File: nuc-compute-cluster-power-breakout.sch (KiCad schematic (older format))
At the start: 20 parts, among them J10 10107844-002LF, J2 BM04B-SRSS-TB-LF-SN, J3 BM04B-SRSS-TB-LF-SN, J5 430450812, J6 430450812, J7 430450812, J8 430450812, J9 430450812, Q11 BC856,215

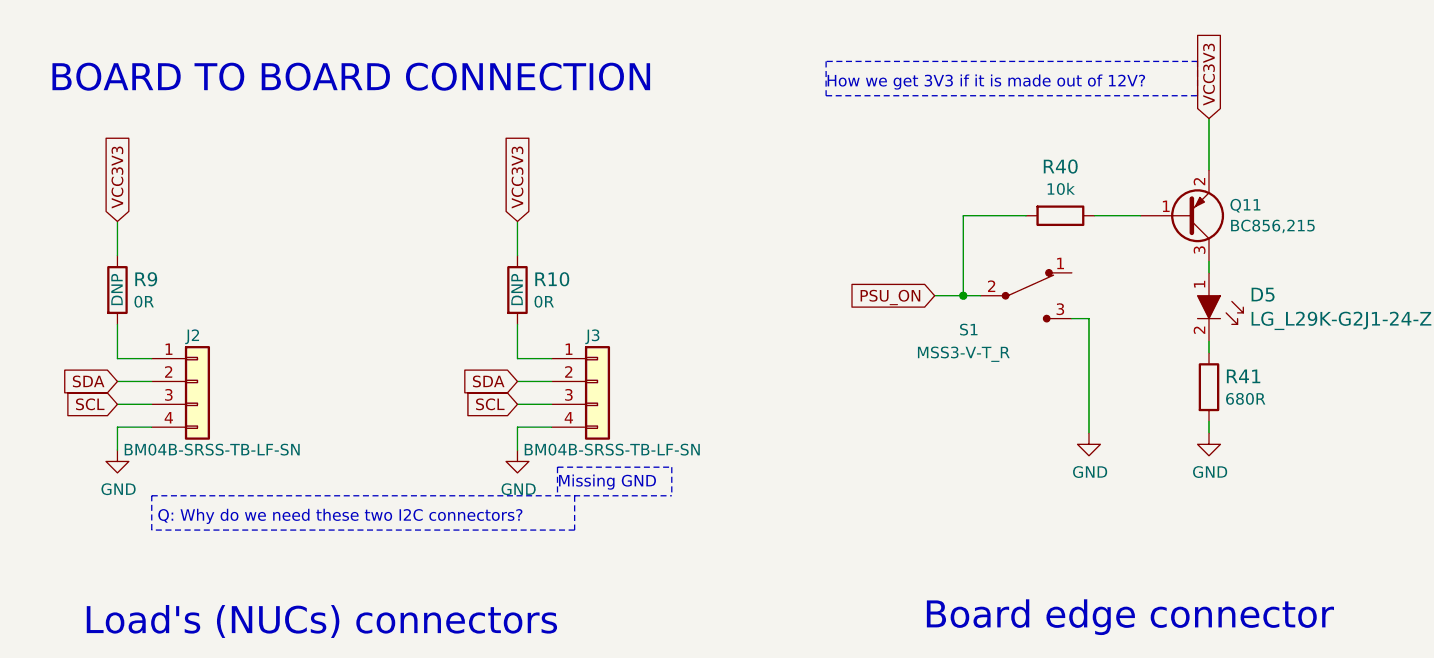
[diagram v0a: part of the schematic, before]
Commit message: Schematic visual update
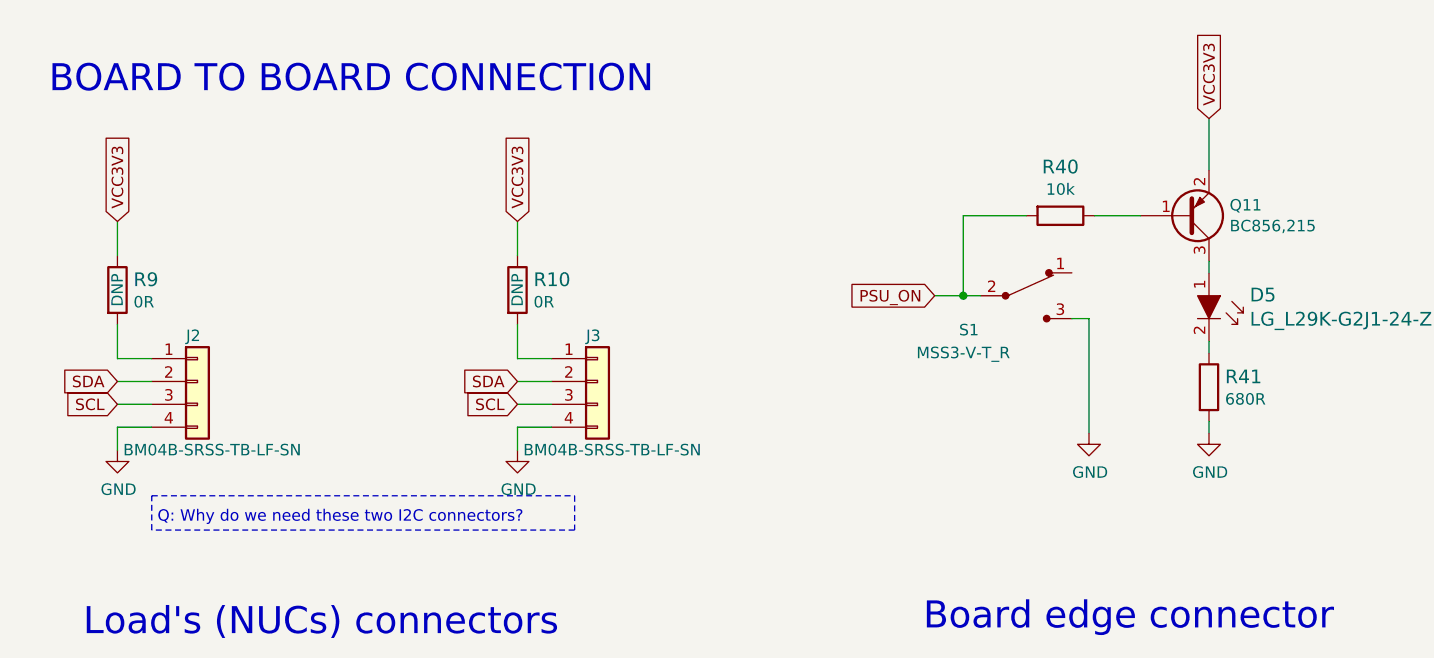
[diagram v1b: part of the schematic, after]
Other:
- note removed: "How we get 3V3 if it is made out of 12V?"
- note removed: "Missing GND"
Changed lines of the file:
@@
 Wire Wire Line
 	7800 6000 7800 5775
-Text Notes 3350 2600 0    50   ~ 0
-Missing GND
-Text Notes 4525 850  0    50   ~ 0
-How we get 3V3 if it is made out of 12V?
 Text Notes 5275 5700 0    50   ~ 0
 Add tespads for the signall pins
@@
 Wire Notes Line
 	1575 2775 1575 2625
-Wire Notes Line
-	3350 2500 3850 2500
-Wire Notes Line
-	3850 2500 3850 2625
-Wire Notes Line
-	3350 2500 3350 2625
-Wire Notes Line
-	1575 2625 3850 2625
-Wire Notes Line
-	4525 725  4525 875
-Wire Notes Line
-	4525 875  6150 875
-Wire Notes Line
-	6150 875  6150 725
-Wire Notes Line
-	6150 725  4525 725
 Wire Notes Line
 	5250 5600 5250 5750
@@
 	1    0    0    -1
 $EndComp
+Wire Notes Line
+	1575 2625 3425 2625
 $EndSCHEMATC

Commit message: Improvements after review
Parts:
- added TP_S1, TP_S10, TP_S11, TP_S12, TP_S16, TP_S17, TP_S18, TP_S19, TP_S2, TP_S20, TP_S21, TP_S22, TP_S23, TP_S24, TP_S3, TP_S4, TP_S5, TP_S6, TP_S7, TP_S8, TP_S9, TP_S_ON: TP_SMD1MM, antmicro-footprints:Testpoint_smd_1mm, symbol antmicroTestPoints:TP_SMD1MM
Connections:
- net PSU_ON: now also TP_S_ON.1; no longer J10.S13, J10.S14, J10.S15
- net at J10.S1: now also TP_S1.1
- net at J10.S10: now also TP_S10.1
- net at J10.S11: now also TP_S11.1
- net at J10.S12: now also TP_S12.1
- net at J10.S16: now also TP_S16.1
- net at J10.S17: now also TP_S17.1
- net at J10.S18: now also TP_S18.1
- net at J10.S19: now also TP_S19.1
- net at J10.S2: now also TP_S2.1
- net at J10.S20: now also TP_S20.1
- net at J10.S21: now also TP_S21.1
- net at J10.S22: now also TP_S22.1
- net at J10.S23: now also TP_S23.1
- net at J10.S24: now also TP_S24.1
- net at J10.S3: now also TP_S3.1
- net at J10.S4: now also TP_S4.1
- net at J10.S5: now also TP_S5.1
- net at J10.S6: now also TP_S6.1
- net at J10.S7: now also TP_S7.1
- net at J10.S8: now also TP_S8.1
- net at J10.S9: now also TP_S9.1
- new net: J10.S13, J10.S14, J10.S15
- no-connect marks 22 -> 1
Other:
- note removed: "Add tespads for the signall pins"
- note removed: "Q: Why do we need these two I2C connectors?"

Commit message: Patches after 2nd revision
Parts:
- removed MP1: PCB_Mount_Hole_3mm_6mm_pad, nuc-compute-cluster-power-breakout-footprints:mounting-hole-3.2mm, symbol nuc-compute-cluster-power-breakout:PCB_Mount_Hole_3mm_6mm_pad
- J2: DNP (none) -> DNP
- renumbered MP5 to MP1, TP_S_ON to TP_S_ON1
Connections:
- net PSU_ON: now also J10.S13, J10.S14, J10.S15
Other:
- moved on the sheet: MP1
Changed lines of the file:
@@
 F 4 "BM04B-SRSS-TB(LF)(SN) " H 1675 1925 50  0001 L CNN "MPN"
 F 5 "JST" H 1675 1825 50  0001 L CNN "Manufacturer"
+F 6 "DNP" V 1875 2375 50  0000 C CNN "DNP"
 	1    1775 2275
 	1    0    0    -1
@@
 	6200 975  6200 1200
 $Comp
-L nuc-compute-cluster-power-breakout:PCB_Mount_Hole_3mm_6mm_pad MP1
-U 1 1 624D5C25
-P 8575 5375
-F 0 "MP1" H 8643 5720 50  0000 C CNN
-F 1 "PCB_Mount_Hole_3mm_6mm_pad" H 8643 5629 50  0000 C CNN
-F 2 "nuc-compute-cluster-power-breakout-footprints:mounting-hole-3.2mm" H 9375 6075 50  0001 C CNN
-F 3 "" H 9525 6175 50  0001 C CNN
-	1    8575 5375
-	1    0    0    -1
-$EndComp
-$Comp
-L nuc-compute-cluster-power-breakout:PCB_Mount_Hole_3mm_6mm_pad MP3
-U 1 1 624DA217
-P 9925 5375
-F 0 "MP3" H 9993 5720 50  0000 C CNN
-F 1 "PCB_Mount_Hole_3mm_6mm_pad" H 9993 5629 50  0000 C CNN
-F 2 "nuc-compute-cluster-power-breakout-footprints:mounting-hole-3.2mm" H 10725 6075 50  0001 C CNN
-F 3 "" H 10875 6175 50  0001 C CNN
-	1    9925 5375
-	1    0    0    -1
-$EndComp
-$Comp
 L nuc-compute-cluster-power-breakout:PCB_Mount_Hole_3mm_6mm_pad MP2
 U 1 1 624E49B1
@@
 $EndComp
 $Comp
-L nuc-compute-cluster-power-breakout:GND #PWR072
-U 1 1 624EAD7E
-P 8875 5575
-F 0 "#PWR072" H 8875 5325 50  0001 C CNN
-F 1 "GND" H 8880 5402 50  0000 C CNN
-F 2 "" H 8875 5575 50  0001 C CNN
-F 3 "" H 8875 5575 50  0001 C CNN
-	1    8875 5575
-	1    0    0    -1
-$EndComp
-$Comp
 L nuc-compute-cluster-power-breakout:GND #PWR074
 U 1 1 624EB150
@@
 	10225 5375 10225 5575
 Wire Wire Line
-	8875 5575 8875 5375
-Wire Wire Line
 	10225 6125 10225 6300
 Wire Wire Line
 	8875 6125 8875 6300
 $Comp
-L nuc-compute-cluster-power-breakout:PCB_Mount_Hole_3mm_6mm_pad MP5
+L nuc-compute-cluster-power-breakout:PCB_Mount_Hole_3mm_6mm_pad MP1
 U 1 1 62504F51
-P 7500 5775
-F 0 "MP5" H 7568 6120 50  0000 C CNN
-F 1 "PCB_Mount_Hole_3mm_6mm_pad" H 7568 6029 50  0000 C CNN
-F 2 "nuc-compute-cluster-power-breakout-footprints:mounting-hole-3.2mm" H 8300 6475 50  0001 C CNN
-F 3 "" H 8450 6575 50  0001 C CNN
-	1    7500 5775
+P 8575 5375
+F 0 "MP1" H 8643 5720 50  0000 C CNN
+F 1 "PCB_Mount_Hole_3mm_6mm_pad" H 8643 5629 50  0000 C CNN
+F 2 "nuc-compute-cluster-power-breakout-footprints:mounting-hole-3.2mm" H 9375 6075 50  0001 C CNN
+F 3 "" H 9525 6175 50  0001 C CNN
+	1    8575 5375
 	1    0    0    -1
 $EndComp
@@
 L nuc-compute-cluster-power-breakout:GND #PWR0106
 U 1 1 6250AA38
-P 7800 6000
-F 0 "#PWR0106" H 7800 5750 50  0001 C CNN
-F 1 "GND" H 7805 5827 50  0000 C CNN
-F 2 "" H 7800 6000 50  0001 C CNN
-F 3 "" H 7800 6000 50  0001 C CNN
-	1    7800 6000
+P 8875 5575
+F 0 "#PWR0106" H 8875 5325 50  0001 C CNN
+F 1 "GND" H 8880 5402 50  0000 C CNN
+F 2 "" H 8875 5575 50  0001 C CNN
+F 3 "" H 8875 5575 50  0001 C CNN
+	1    8875 5575
 	1    0    0    -1
 $EndComp
-Wire Wire Line
-	7800 6000 7800 5775
 $Comp
-L nuc-compute-cluster-power-breakout:GND #PWR?
+L nuc-compute-cluster-power-breakout:GND #PWR0107
 U 1 1 624F066D
 P 3175 2425
-F 0 "#PWR?" H 3175 2175 50  0001 C CNN
+F 0 "#PWR0107" H 3175 2175 50  0001 C CNN
 F 1 "GND" H 3180 2252 50  0000 C CNN
 F 2 "" H 3175 2425 50  0001 C CNN
@@
 	5175 5400 5300 5400
 $Comp
-L antmicroTestPoints:TP_SMD1MM TP_S_ON
+L antmicroTestPoints:TP_SMD1MM TP_S_ON1
 U 1 1 625B2FF0
 P 6725 5400
-F 0 "TP_S_ON" H 6775 5400 50  0000 L CNN
+F 0 "TP_S_ON1" H 6775 5400 50  0000 L CNN
 F 1 "TP_SMD1MM" H 6725 5300 50  0001 C CNN
 F 2 "antmicro-footprints:Testpoint_smd_1mm" H 6925 5600 60  0001 L CNN
@@
 	1    0    0    -1
 $EndComp
-Wire Wire Line
-	6725 5300 6525 5300
 Connection ~ 6725 5300
 Wire Wire Line
 	6725 5300 6900 5300
+Wire Wire Line
+	6500 5300 6725 5300
+$Comp
+L nuc-compute-cluster-power-breakout:PCB_Mount_Hole_3mm_6mm_pad MP3
+U 1 1 624DA217
+P 9925 5375
+F 0 "MP3" H 9993 5720 50  0000 C CNN
+F 1 "PCB_Mount_Hole_3mm_6mm_pad" H 9993 5629 50  0000 C CNN
+F 2 "nuc-compute-cluster-power-breakout-footprints:mounting-hole-3.2mm" H 10725 6075 50  0001 C CNN
+F 3 "" H 10875 6175 50  0001 C CNN
+	1    9925 5375
+	1    0    0    -1
+$EndComp
+Wire Wire Line
+	8875 5575 8875 5375
 $EndSCHEMATC

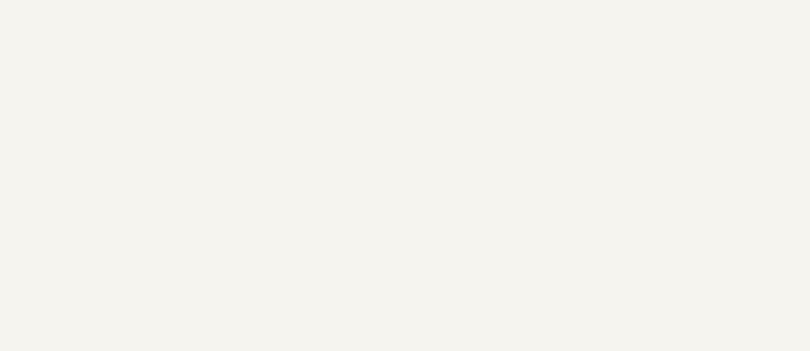
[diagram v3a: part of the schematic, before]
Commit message: Added board cut-out. Logos replacement
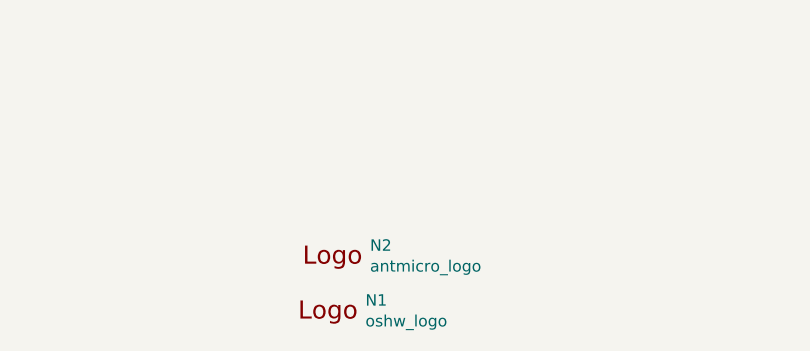
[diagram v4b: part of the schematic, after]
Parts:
- added N1: oshw_logo, antmicro-footprints:OSHW-Logo_7.5x8mm_Mask, symbol antmicroMechanicalParts:oshw_logo
- added N2: antmicro_logo, antmicro-footprints:antmicro-logo_scaled_20mm_mask, symbol antmicroMechanicalParts:antmicro_logo
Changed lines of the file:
@@
 Wire Wire Line
 	8875 5575 8875 5375
+$Comp
+L antmicroMechanicalParts:antmicro_logo N2
+U 1 1 62508F0C
+P 6075 7100
+F 0 "N2" H 6289 7193 50  0000 L CNN
+F 1 "antmicro_logo" H 6289 7102 50  0000 L CNN
+F 2 "antmicro-footprints:antmicro-logo_scaled_20mm_mask" H 5975 7350 50  0001 C CNN
+F 3 "" H 6075 7450 50  0001 C CNN
+	1    6075 7100
+	1    0    0    -1
+$EndComp
+$Comp
+L antmicroMechanicalParts:oshw_logo N1
+U 1 1 6250A4B1
+P 6075 7250
+F 0 "N1" H 6269 7253 50  0000 L CNN
+F 1 "oshw_logo" H 6269 7162 50  0000 L CNN
+F 2 "antmicro-footprints:OSHW-Logo_7.5x8mm_Mask" H 6095 7010 50  0001 C CNN
+F 3 "" H 6075 7250 50  0001 C CNN
+	1    6075 7250
+	1    0    0    -1
+$EndComp
 $EndSCHEMATC

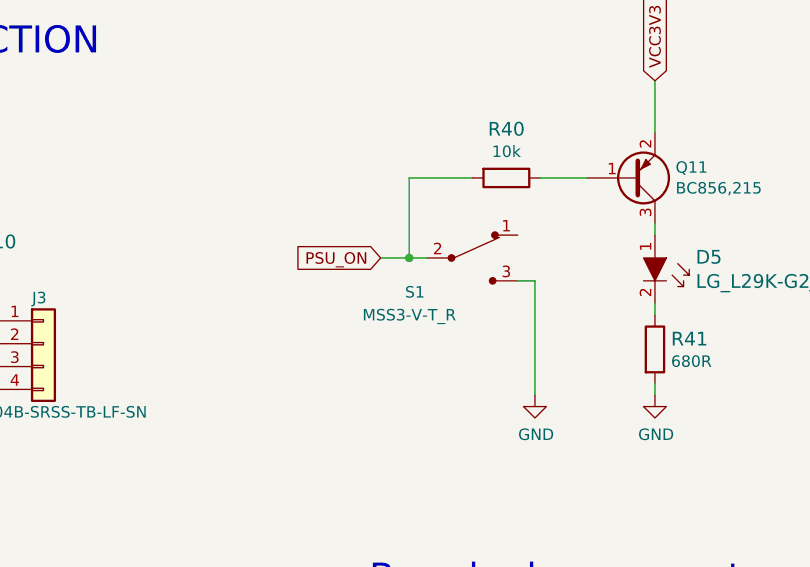
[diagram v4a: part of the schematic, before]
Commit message: Add R45 to implement ALWAYS ON feature
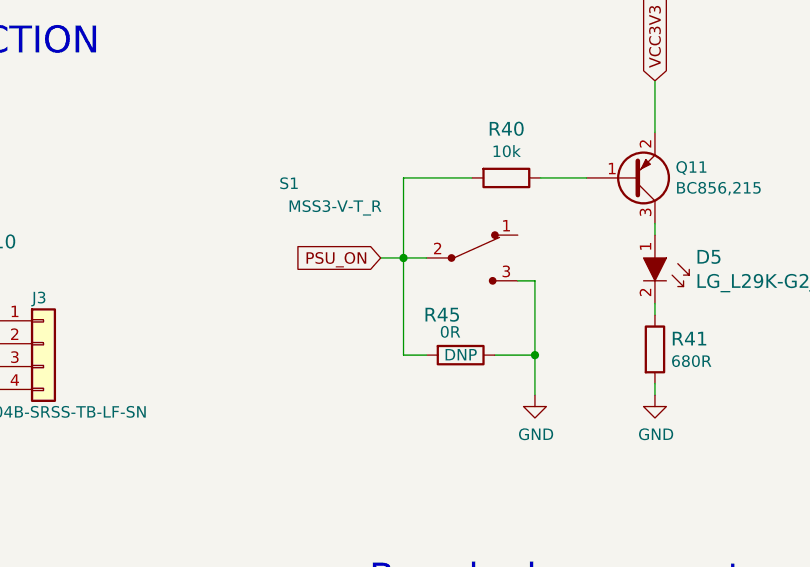
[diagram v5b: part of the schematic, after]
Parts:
- added R45: R_0R_0402, nuc-compute-cluster-power-breakout-footprints:0402-res, symbol nuc-compute-cluster-power-breakout:R_0R_0402
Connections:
- net GND: now also R45.1
- net PSU_ON: now also R45.2
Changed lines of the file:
@@
 U 1 1 6270AED7
 P 5400 1750
-F 0 "S1" H 5150 1600 50  0000 C CNN
-F 1 "MSS3-V-T_R" H 5125 1500 50  0000 C CNN
+F 0 "S1" H 4600 2075 50  0000 C CNN
+F 1 "MSS3-V-T_R" H 4800 1975 50  0000 C CNN
 F 2 "nuc-compute-cluster-power-breakout-footprints:Switch_Slide_MSS3" H 5600 1950 50  0001 L CNN
 F 3 "https://pl.mouser.com/datasheet/2/910/605_MSS34-1571494.pdf" H 5600 2050 60  0001 L CNN
@@
 $EndComp
 Wire Wire Line
-	5000 1750 5125 1750
+	5000 1750 5100 1750
 Wire Wire Line
 	5675 1850 5600 1850
 Wire Wire Line
-	5125 1750 5125 1400
-Connection ~ 5125 1750
-Wire Wire Line
-	5125 1750 5200 1750
+	5100 1750 5100 1400
+Connection ~ 5100 1750
+Wire Wire Line
+	5100 1750 5200 1750
 $Comp
 L nuc-compute-cluster-power-breakout:GND #PWR071
@@
 $EndComp
 Wire Wire Line
-	5125 1400 5400 1400
+	5100 1400 5400 1400
 Wire Wire Line
 	5700 1400 5900 1400
@@
 $EndComp
 Wire Wire Line
-	5675 1850 5675 2350
+	5675 1850 5675 2175
 $Comp
 L nuc-compute-cluster-power-breakout:BC856,215 Q11
@@
 	1    0    0    -1
 $EndComp
+$Comp
+L nuc-compute-cluster-power-breakout:R_0R_0402 R45
+U 1 1 6263D1AF
+P 5350 2175
+F 0 "R45" H 5350 2000 60  0000 L CNN
+F 1 "R_0R_0402" H 5350 2025 60  0001 C CNN
+F 2 "nuc-compute-cluster-power-breakout-footprints:0402-res" H 5550 2375 60  0001 L CNN
+F 3 "" H 5350 2175 50  0001 C CNN
+F 4 "PANASONIC" H 5550 2575 60  0001 L CNN "Manufacturer"
+F 5 "ERJ2GE0R00X" H 5550 2475 60  0001 L CNN "MPN"
+F 6 "0R" H 5350 2075 50  0000 L CNN "Val"
+F 7 "DNP" H 5350 2175 50  0000 C CNN "DNP"
+	1    5350 2175
+	-1   0    0    1
+$EndComp
+Wire Wire Line
+	5500 2175 5675 2175
+Connection ~ 5675 2175
+Wire Wire Line
+	5675 2175 5675 2350
+Wire Wire Line
+	5200 2175 5100 2175
+Wire Wire Line
+	5100 2175 5100 1750
 $EndSCHEMATC

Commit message: Performed loclib
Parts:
- N1: footprint antmicro-footprints:OSHW-Logo_7.5x8mm_Mask -> nuc-compute-cluster-power-breakout-footprints:OSHW-Logo_7.5x8mm_Mask; symbol antmicroMechanicalParts:oshw_logo -> nuc-compute-cluster-power-breakout:oshw_logo
- N2: footprint antmicro-footprints:antmicro-logo_scaled_20mm_mask -> nuc-compute-cluster-power-breakout-footprints:antmicro-logo_scaled_20mm_mask; symbol antmicroMechanicalParts:antmicro_logo -> nuc-compute-cluster-power-breakout:antmicro_logo
- TP_S1, TP_S10, TP_S11, TP_S12, TP_S16, TP_S17, TP_S18, TP_S19, TP_S2, TP_S20, TP_S21, TP_S22, TP_S23, TP_S24, TP_S3, TP_S4, TP_S5, TP_S6, TP_S7, TP_S8, TP_S9, TP_S_ON1: footprint antmicro-footprints:Testpoint_smd_1mm -> nuc-compute-cluster-power-breakout-footprints:Testpoint_smd_1mm; symbol antmicroTestPoints:TP_SMD1MM -> nuc-compute-cluster-power-breakout:TP_SMD1MM
